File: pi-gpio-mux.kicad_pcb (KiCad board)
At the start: 2 copper layers, 65 x 56 mm, 35 parts, among them J1 Raspberry_Pi_2_3, J2 Raw, J3 Buffered, J4 Register-1, J5 Register-2, J6 Clk1, J7 Clk1, U1 74AHCT245, U10 74AHCT574, U11 74AHCT574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

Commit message: Even placement.
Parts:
- moved C8 2.45 mm to (254.4, 125.6), turned to 90 degrees
- moved C4 2.45 mm to (254.4, 112.2), turned to 270 degrees
- moved C12 2.43 mm to (254.4, 138.9), turned to 90 degrees
- moved C7 2.10 mm to (244.2, 125.6), turned to 90 degrees
- moved C3 2.10 mm to (244.2, 112.2), turned to 270 degrees
- moved U12 2.09 mm to (249.1, 138.9)
- moved U4 2.09 mm to (249.1, 112.2)
- moved U8 2.09 mm to (249.1, 125.6)
- moved C11 2.08 mm to (244.2, 138.9), turned to 90 degrees
- moved C6 1.75 mm to (234.1, 125.6), turned to 270 degrees
- moved C2 1.75 mm to (234.1, 112.2), turned to 270 degrees
- moved C10 1.72 mm to (234.1, 138.9), turned to 90 degrees
- moved U11 1.71 mm to (238.9, 138.9)
- moved U3 1.71 mm to (238.9, 112.2)
- moved U7 1.71 mm to (238.9, 125.6)
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
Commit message: Basic fan-out.
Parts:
- turned C6 to 90 degrees
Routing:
- net GND: track 0.00 -> 128.3 mm
- net Pin40-GPIO21: track 0.00 -> 15.3 mm
- net Pin36-GPIO16: track 0.00 -> 15.3 mm
- net Pin38-GPIO20: track 0.00 -> 15.3 mm
- net VCC: track 0.00 -> 15.1 mm
- net Pin28-GPIO1: track 0.00 -> 13.2 mm
- net Pin12-GPIO18: track 0.00 -> 12.0 mm
- net Pin10-GPIO15: track 0.00 -> 12.0 mm
- net Pin31-GPIO6: track 0.00 -> 10.7 mm
- net Pin29-GPIO5: track 0.00 -> 10.7 mm
- net Pin32-GPIO12: track 0.00 -> 10.7 mm
- net Pin3-GPIO2: track 0.00 -> 9.64 mm
- net Pin22-GPIO25: track 0.00 -> 9.62 mm
- net Pin21-GPIO9: track 0.00 -> 9.62 mm
- net Pin24-GPIO8: track 0.00 -> 9.62 mm
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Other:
- net class Default: via_dia 1 -> 0.8
- rule via_min_size: 0.8 -> 0.7

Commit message: First layout template vias.
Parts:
- J7: value Clk1 -> Clk2
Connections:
- net Net-(J6-Pad1) renamed /CLK1
- net Net-(J7-Pad1) renamed /CLK2
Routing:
- net VCC: track 15.1 -> 32.4 mm, vias 0 -> 2
- net /CLK2: track 0.00 -> 17.1 mm, vias 0 -> 2
- net Pin13-GPIO27: track 6.03 -> 16.6 mm, vias 0 -> 1
- net Pin11-GPIO17: track 6.03 -> 16.1 mm, vias 0 -> 1
- net Pin5-GPIO3: track 6.04 -> 15.8 mm, vias 0 -> 1
- net Pin8-GPIO14: track 8.58 -> 17.4 mm, vias 0 -> 1
- net Pin24-GPIO8: track 9.62 -> 18.2 mm, vias 0 -> 1
- net Pin12-GPIO18: track 12.0 -> 19.8 mm, vias 0 -> 1
- net Pin22-GPIO25: track 9.62 -> 17.4 mm, vias 0 -> 1
- net Pin18-GPIO24: track 8.57 -> 15.8 mm, vias 0 -> 1
- net Pin3-GPIO2: track 9.64 -> 16.3 mm, vias 0 -> 1
- net Pin10-GPIO15: track 12.0 -> 18.4 mm, vias 0 -> 1
- net Pin7-GPIO4: track 8.58 -> 14.8 mm, vias 0 -> 1
- net Pin15-GPIO22: track 8.57 -> 13.7 mm
- net Pin23-GPIO11: track 9.62 -> 14.7 mm
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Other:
- rule via_min_drill: 0.5 -> 0.4

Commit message: Replicate template.
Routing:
- net VCC: track 32.4 -> 75.5 mm, vias 2 -> 16
- net /CLK1: track 0.00 -> 19.6 mm, vias 0 -> 6
- net User3: track 0.00 -> 9.97 mm, vias 0 -> 4
- net Pin36-GPIO16: track 15.3 -> 20.8 mm, vias 0 -> 2
- net Pin23-GPIO11: track 14.7 -> 20.2 mm, vias 0 -> 2
- net Pin32-GPIO12: track 10.7 -> 15.2 mm, vias 0 -> 2
- net Pin22-GPIO25: track 17.4 -> 21.9 mm, vias 1 -> 3
- net User2: track 0.00 -> 4.55 mm, vias 0 -> 2
- net Pin33-GPIO13: track 8.61 -> 13.1 mm, vias 0 -> 2
- net Pin24-GPIO8: track 18.2 -> 22.7 mm, vias 1 -> 3
- net Pin35-GPIO19: track 8.61 -> 12.8 mm, vias 0 -> 2
- net Pin26-GPIO7: track 9.62 -> 13.8 mm, vias 0 -> 2
- net Pin16-GPIO23: track 8.57 -> 12.8 mm, vias 0 -> 2
- net Pin31-GPIO6: track 10.7 -> 14.6 mm, vias 0 -> 2
- net Pin21-GPIO9: track 14.1 -> 18.0 mm, vias 0 -> 2
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
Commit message: Power and clock routing for Registers.
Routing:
- net VCC: track 75.5 -> 141.5 mm
- net /CLK2: track 19.6 -> 51.0 mm
- net /CLK1: track 19.6 -> 40.5 mm
- net Pin26-GPIO7: track 13.8 -> 15.0 mm

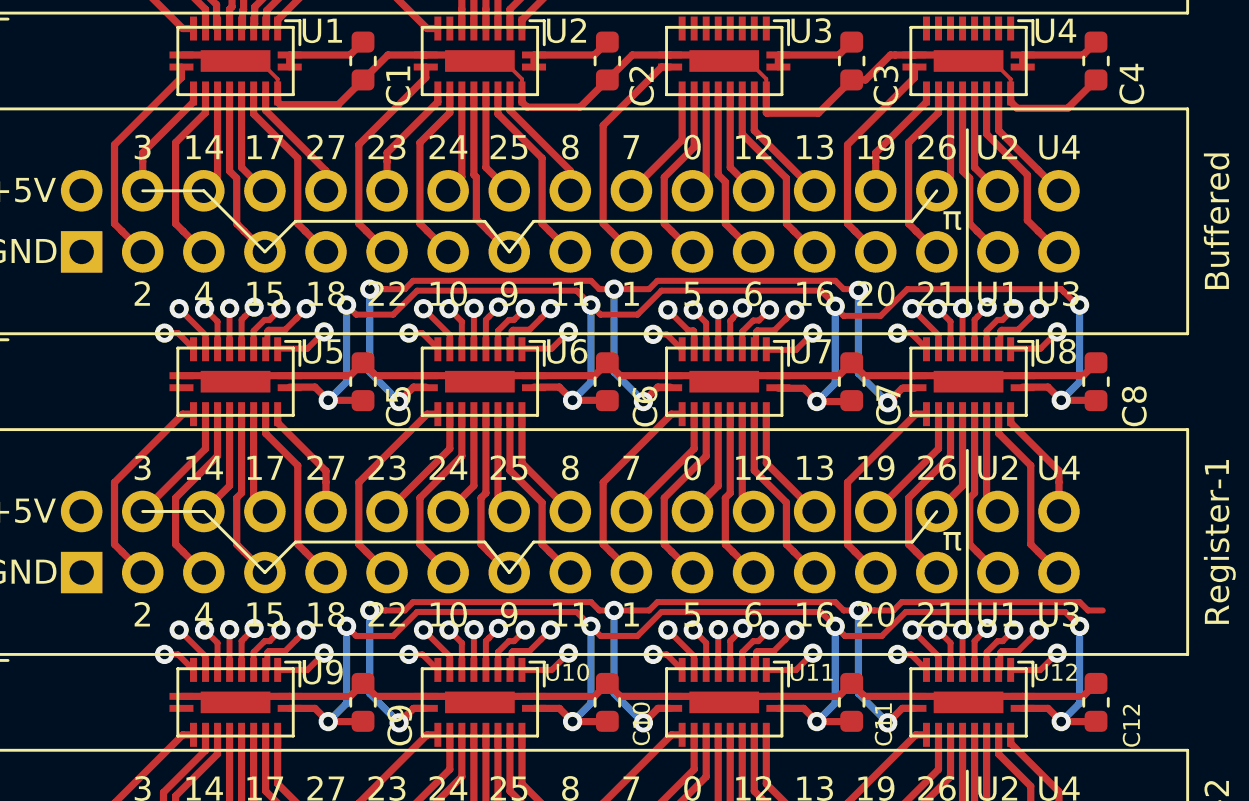
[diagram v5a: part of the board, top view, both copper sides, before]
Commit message: trace signal between connectors.
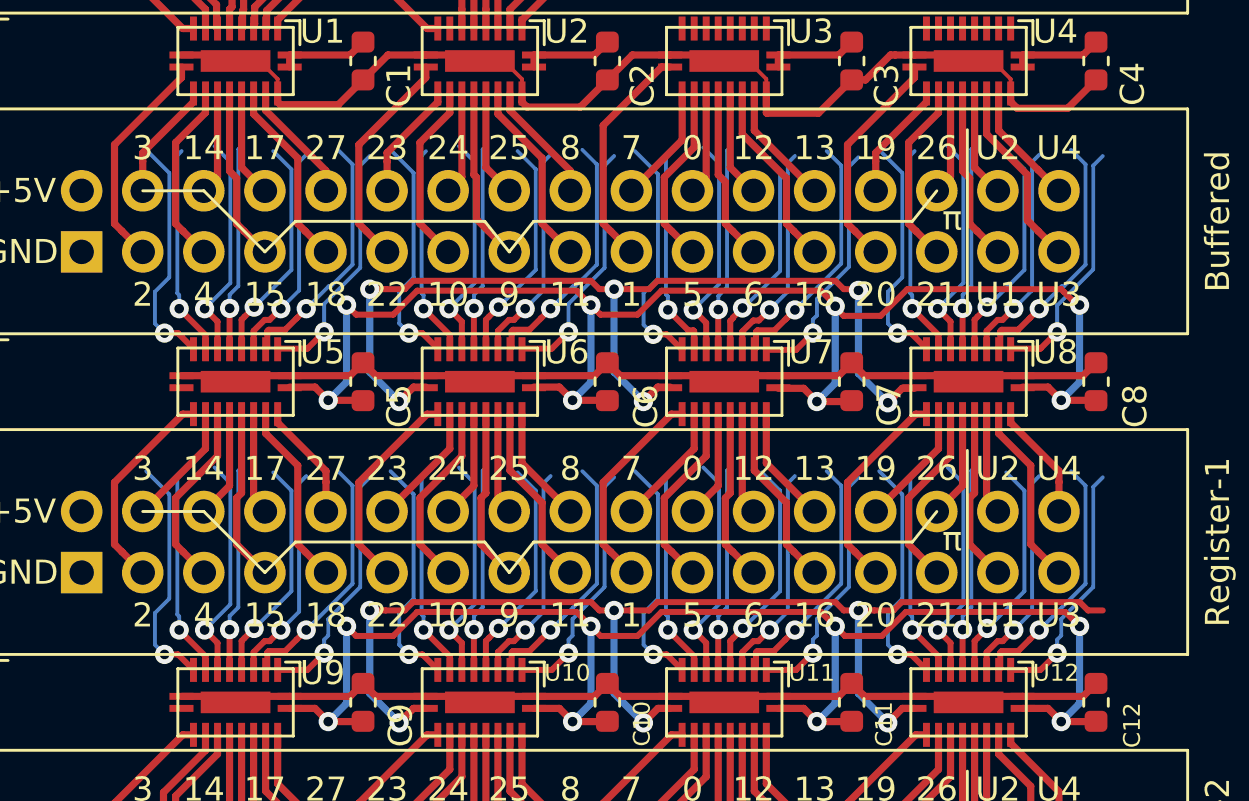
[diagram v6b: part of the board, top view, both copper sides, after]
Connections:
- U12 pad 2: User3 -> User4
- U4 pad 2: User3 -> User4
- U8 pad 2: User3 -> User4
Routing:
- net User4: track 0.00 -> 20.6 mm, vias 0 -> 2
- net Pin3-GPIO2: track 17.8 -> 34.6 mm
- net Pin15-GPIO22: track 16.7 -> 33.6 mm
- net Pin38-GPIO20: track 18.2 -> 35.1 mm
- net Pin28-GPIO1: track 16.2 -> 33.0 mm
- net Pin13-GPIO27: track 18.9 -> 35.1 mm
- net Pin24-GPIO8: track 22.7 -> 38.9 mm
- net Pin33-GPIO13: track 13.1 -> 29.3 mm
- net Pin12-GPIO18: track 22.6 -> 38.0 mm
- net Pin23-GPIO11: track 20.2 -> 35.6 mm
- net Pin36-GPIO16: track 21.0 -> 36.3 mm
- net Pin7-GPIO4: track 16.6 -> 31.6 mm
- net Pin19-GPIO10: track 17.7 -> 32.6 mm
- net Pin40-GPIO21: track 19.0 -> 34.0 mm
- net Pin29-GPIO5: track 14.4 -> 29.4 mm
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
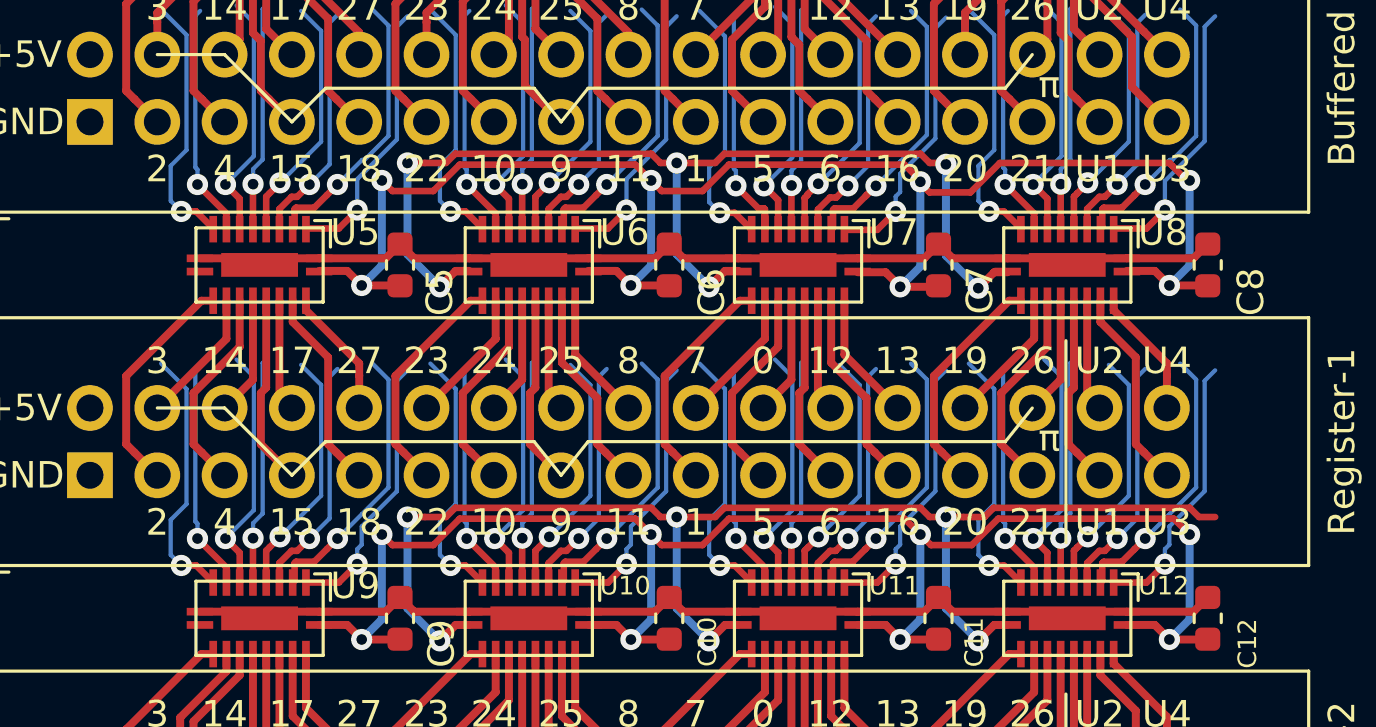
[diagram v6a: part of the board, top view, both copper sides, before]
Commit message: Bus connect between registers.
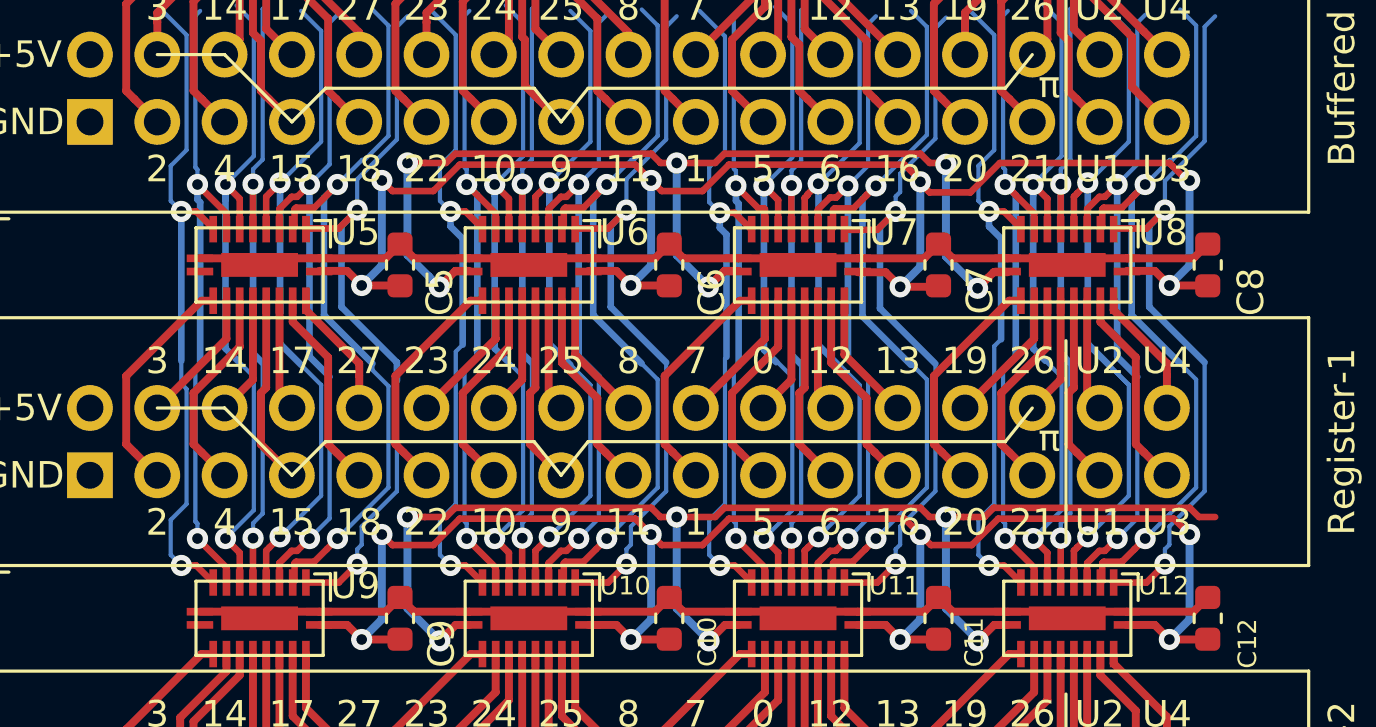
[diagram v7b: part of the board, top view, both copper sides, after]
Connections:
- J2 pad 34: User3 -> User4
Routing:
- net Pin31-GPIO6: track 29.5 -> 37.7 mm
- net User1: track 18.8 -> 27.0 mm
- net Pin21-GPIO9: track 32.8 -> 41.1 mm
- net User3: track 20.9 -> 28.6 mm
- net Pin36-GPIO16: track 36.3 -> 44.0 mm
- net Pin12-GPIO18: track 38.0 -> 45.7 mm
- net Pin23-GPIO11: track 35.6 -> 43.3 mm
- net Pin10-GPIO15: track 35.2 -> 42.4 mm
- net Pin22-GPIO25: track 35.6 -> 42.8 mm
- net Pin11-GPIO17: track 32.0 -> 39.2 mm
- net Pin32-GPIO12: track 28.9 -> 36.1 mm
- net User2: track 18.2 -> 25.4 mm
- net Pin16-GPIO23: track 26.1 -> 33.2 mm
- net Pin35-GPIO19: track 26.2 -> 33.3 mm
- net Pin7-GPIO4: track 31.6 -> 38.6 mm
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
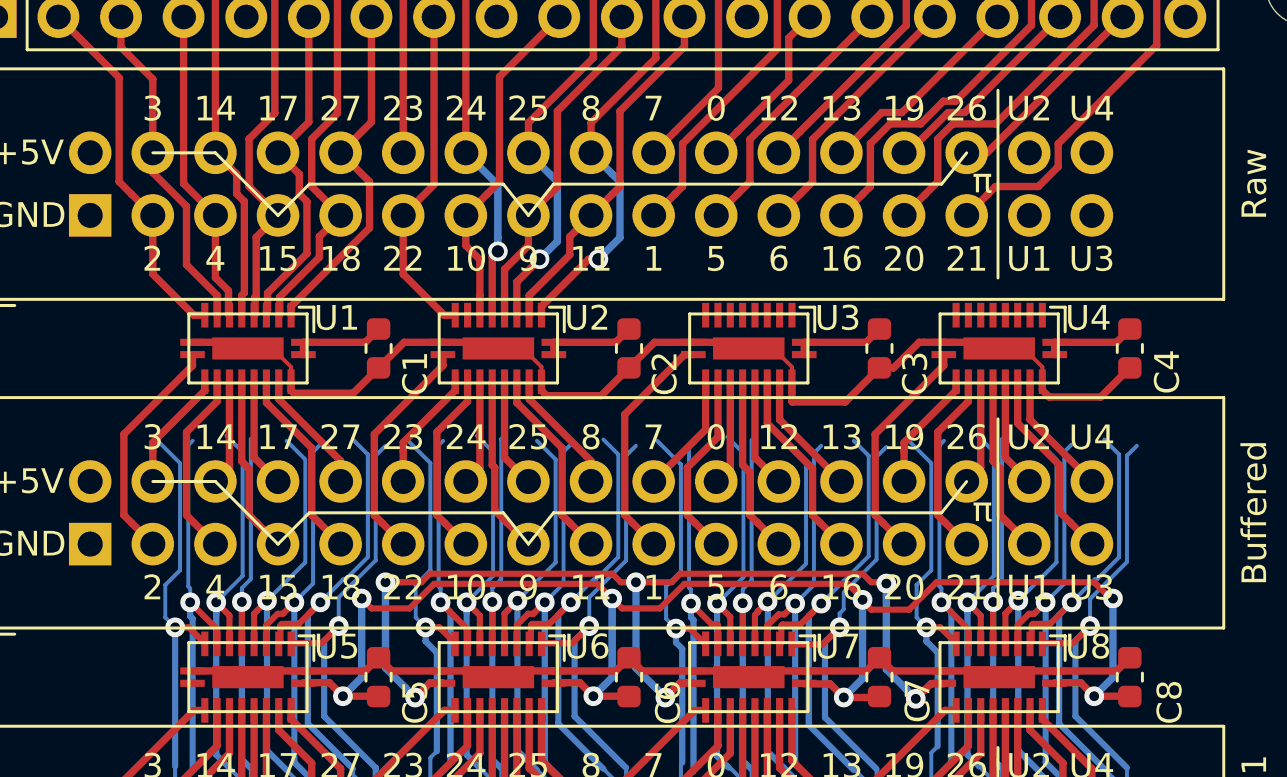
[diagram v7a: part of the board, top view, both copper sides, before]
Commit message: Bus raw -> registers.
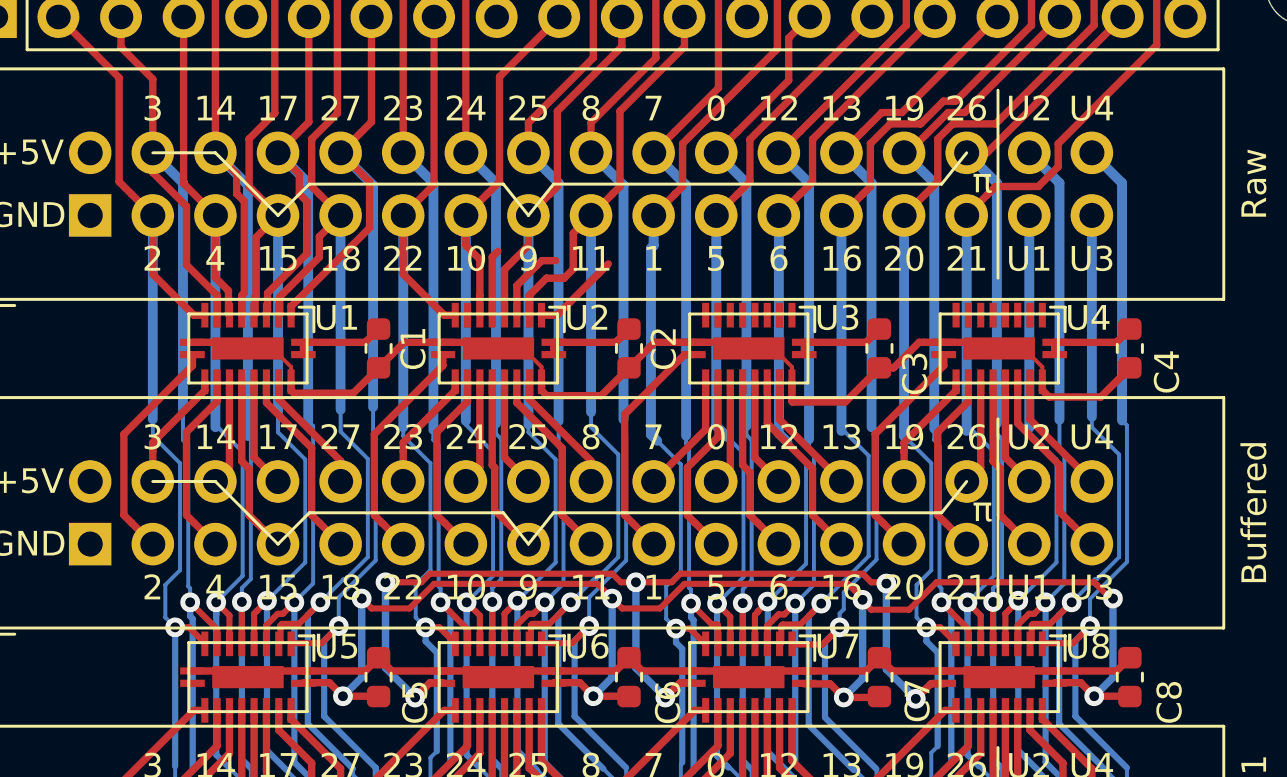
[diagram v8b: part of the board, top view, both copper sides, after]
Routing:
- net Pin33-GPIO13: track 36.2 -> 48.6 mm
- net Pin32-GPIO12: track 36.1 -> 48.4 mm
- net User4: track 27.6 -> 40.0 mm
- net Pin13-GPIO27: track 42.1 -> 54.4 mm
- net Pin11-GPIO17: track 39.2 -> 51.5 mm
- net User2: track 25.4 -> 37.7 mm
- net Pin26-GPIO7: track 35.2 -> 47.5 mm
- net Pin5-GPIO3: track 38.1 -> 50.3 mm
- net Pin16-GPIO23: track 33.2 -> 45.4 mm
- net Pin35-GPIO19: track 33.3 -> 45.5 mm
- net Pin27-GPIO0: track 31.0 -> 43.1 mm
- net Pin37-GPIO26: track 32.6 -> 44.6 mm
- net Pin8-GPIO14: track 39.7 -> 51.5 mm
- net Pin23-GPIO11: track 43.3 -> 53.0 mm
- net Pin36-GPIO16: track 44.0 -> 53.4 mm
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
